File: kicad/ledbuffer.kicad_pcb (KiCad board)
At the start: 2 copper layers, 39.4 x 52.1 mm, 0 parts

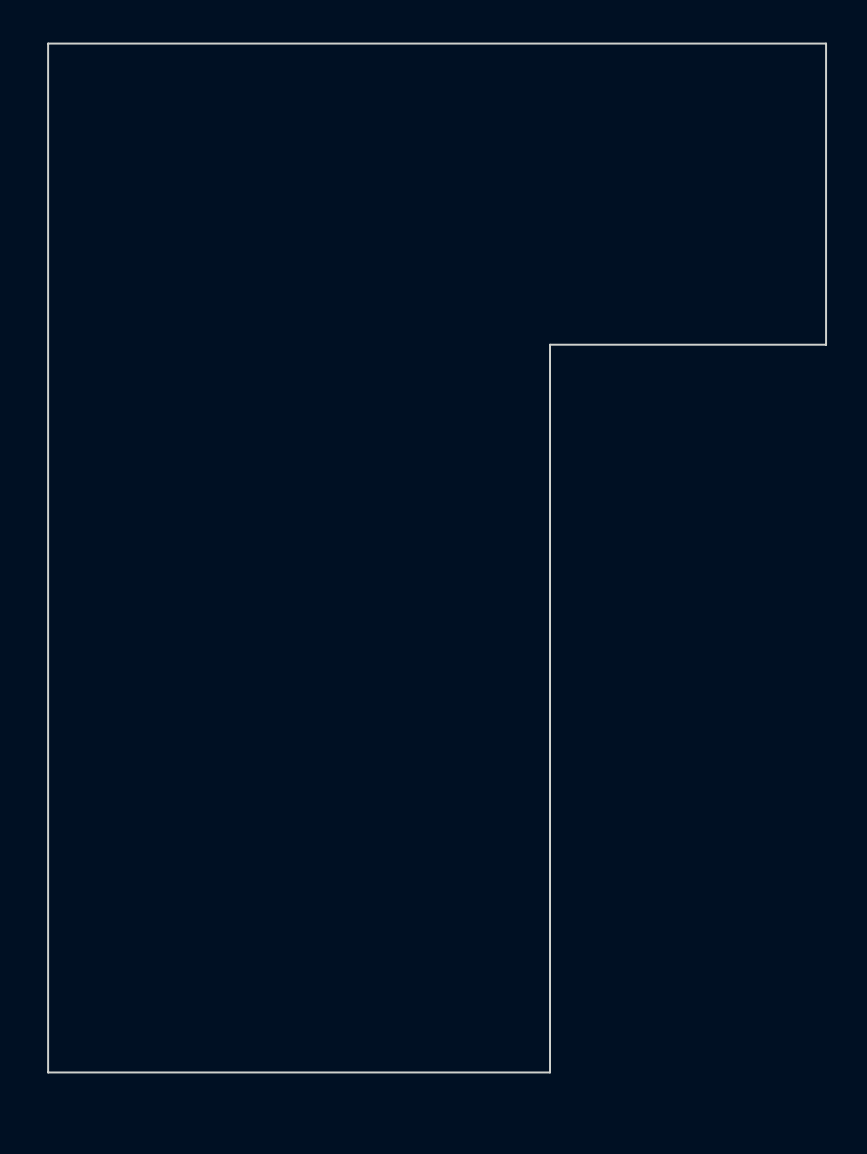
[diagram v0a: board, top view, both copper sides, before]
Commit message: started layout placement by Dharma
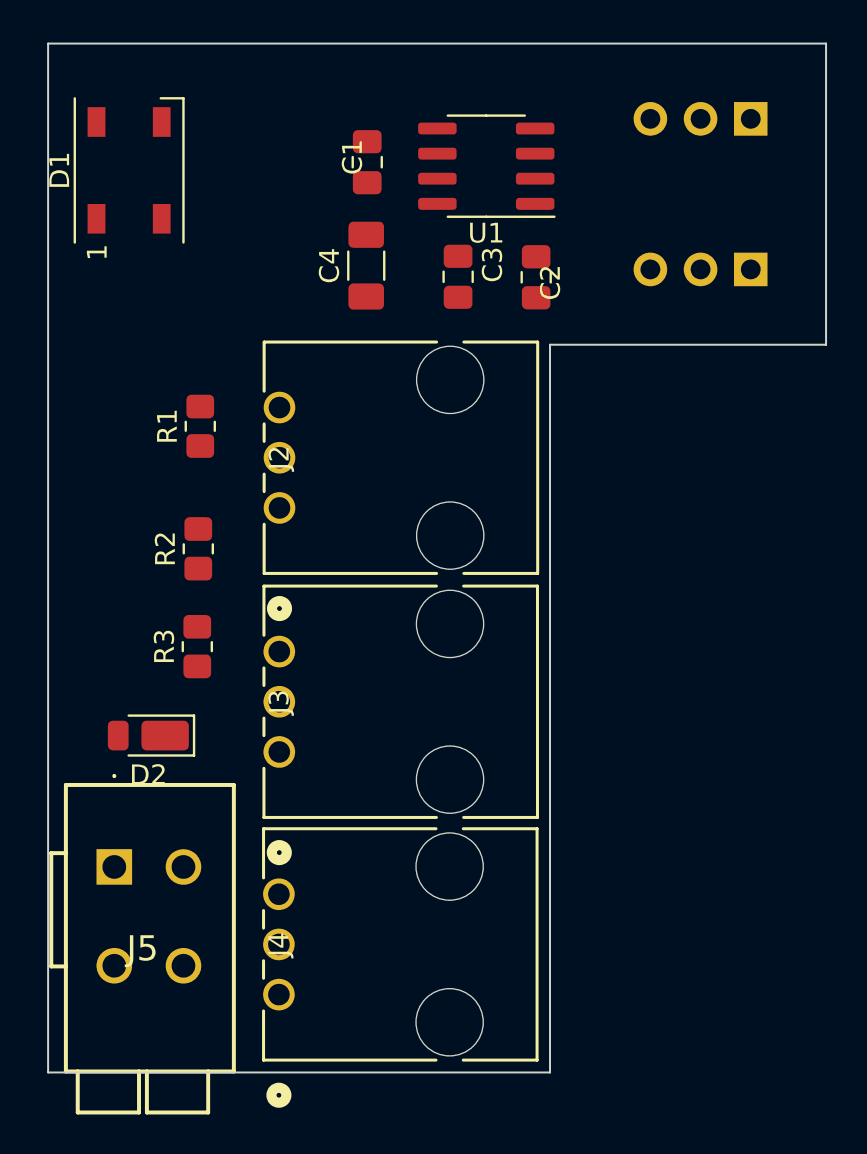
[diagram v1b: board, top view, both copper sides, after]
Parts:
- added C1: 1uF, Capacitor_SMD:C_0805_2012Metric_Pad1.18x1.45mm_HandSolder, F.Cu at (130.4, 55.5)
- added C2: 1uF, Capacitor_SMD:C_0805_2012Metric_Pad1.18x1.45mm_HandSolder, F.Cu at (139.0, 61.4)
- added C3: 1uF, Capacitor_SMD:C_0805_2012Metric_Pad1.18x1.45mm_HandSolder, F.Cu at (135.1, 61.3)
- added C4: 100uF, Capacitor_SMD:C_1206_3216Metric_Pad1.33x1.80mm_HandSolder, F.Cu at (130.4, 60.8)
- added D1: WS2812B, LED_SMD:LED_WS2812B_PLCC4_5.0x5.0mm_P3.2mm, F.Cu at (118.4, 56.0)
- added D2: SBR3U60P1, Diode_SMD:D_PowerDI-123, F.Cu at (119.4, 84.5)
- added J1: Conn_01x03, Connector_PinSocket_2.54mm:PinSocket_1x03_P2.54mm_Vertical, B.Cu at (149.9, 53.3)
- added J2: Conn_01x03, Library:CONN_70555-0002_MOL, F.Cu at (126.0, 73.0)
- added J3: Conn_01x03, Library:CONN_70555-0002_MOL, F.Cu at (126.0, 85.4)
- added J4: Conn_01x03, Library:CONN_70555-0002_MOL, F.Cu at (126.0, 97.7)
- added J5: Conn_01x02, Library:26011102, F.Cu at (117.7, 91.2)
- added J6: Conn_01x03, Connector_PinSocket_2.54mm:PinSocket_1x03_P2.54mm_Vertical, B.Cu at (149.9, 61.0)
- added R1: 100, Resistor_SMD:R_0805_2012Metric_Pad1.20x1.40mm_HandSolder, F.Cu at (122.0, 68.9)
- added R2: 100, Resistor_SMD:R_0805_2012Metric_Pad1.20x1.40mm_HandSolder, F.Cu at (121.9, 75.1)
- added R3: 100, Resistor_SMD:R_0805_2012Metric_Pad1.20x1.40mm_HandSolder, F.Cu at (121.8, 80.0)
- added U1: LM2931-5.0_SO8, Package_SO:SOIC-8_3.9x4.9mm_P1.27mm, F.Cu at (136.5, 55.7)

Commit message: placement tweaks, set up for routing moved a few things a little bit added net+via sizes and net classes a few sample routes
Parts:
- moved C2 22.4 mm to (118.1, 53.3), turned to 0 degrees
- moved C3 10.9 mm to (127.6, 53.3)
- moved C1 9.51 mm to (139.7, 53.3), turned to -90 degrees
- moved C4 9.13 mm to (125.1, 53.3), turned to -90 degrees
- moved D1 3.74 mm to (118.4, 59.7)
- moved U1 3.32 mm to (133.3, 54.6), turned to 0 degrees
- moved D2 0.73 mm to (119.4, 83.8)
- turned R1 to 0 degrees
- turned R2 to 0 degrees
- turned R3 to 0 degrees
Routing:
- net +6V: track 0.00 -> 13.3 mm
- net GND: track 0.00 -> 7.99 mm
- net Net-(D1-DIN): track 0.00 -> 7.18 mm
- net /Vled: track 0.00 -> 4.97 mm

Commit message: added a wire.
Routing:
- net GND: track 7.99 -> 30.5 mm
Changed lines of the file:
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@@
     (stroke (width 0.15) (type default)) (fill none) (layer "User.2"))
   (segment (start 140.97 50.8) (end 144.78 50.8) (width 0.635) (layer "F.Cu") (net 1))
+  (segment (start 139.065 52.705) (end 140.97 50.8) (width 0.635) (layer "F.Cu") (net 1))
   (segment (start 135.825 52.705) (end 139.065 52.705) (width 0.635) (layer "F.Cu") (net 1))
-  (segment (start 139.065 52.705) (end 140.97 50.8) (width 0.635) (layer "F.Cu") (net 1))
   (segment (start 144.78 50.8) (end 147.32 53.34) (width 0.635) (layer "F.Cu") (net 1))
+  (segment (start 149.86 53.34) (end 149.86 60.96) (width 0.635) (layer "F.Cu") (net 2))
   (segment (start 120.51 99.06) (end 124.46 99.06) (width 0.635) (layer "F.Cu") (net 2))
+  (segment (start 140.0332 54.7107) (end 139.7 54.3775) (width 0.635) (layer "F.Cu") (net 2))
+  (segment (start 148.4893 54.7107) (end 140.0332 54.7107) (width 0.635) (layer "F.Cu") (net 2))
+  (segment (start 149.86 53.34) (end 148.4893 54.7107) (width 0.635) (layer "F.Cu") (net 2))
+  (segment (start 139.7 54.3775) (end 136.2275 54.3775) (width 0.635) (layer "F.Cu") (net 2))
+  (segment (start 136.2275 54.3775) (end 135.825 53.975) (width 0.635) (layer "F.Cu") (net 2))
   (segment (start 117.65 96.2) (end 120.51 99.06) (width 0.635) (layer "F.Cu") (net 2))
   (segment (start 144.78 53.34) (end 139.7 58.42) (width 0.254) (layer "B.Cu") (net 5))

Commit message: wires and text
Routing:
- net Net-(D1-DIN): track 7.18 -> 40.0 mm
- net /Vled: track 4.97 -> 37.6 mm
- net GND: track 30.5 -> 0.00 mm
- net +5V: track 0.00 -> 24.3 mm
- net Net-(D1-DOUT): track 0.00 -> 18.4 mm
- net Net-(J4-Pin_3): track 0.00 -> 13.8 mm, vias 0 -> 1
- net Net-(J3-Pin_3): track 0.00 -> 6.48 mm
- net Net-(J2-Pin_3): track 0.00 -> 3.55 mm
- net +6V: track 13.3 -> 12.4 mm
- added copper zone on B.Cu, net GND
- added copper zone on F.Cu, net GND
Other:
- board text added: "M.I.A. - Jake Donovon /dev/mentor0 - Steve Tell THE G.O.A.T. - Dharma Chari-Letts"

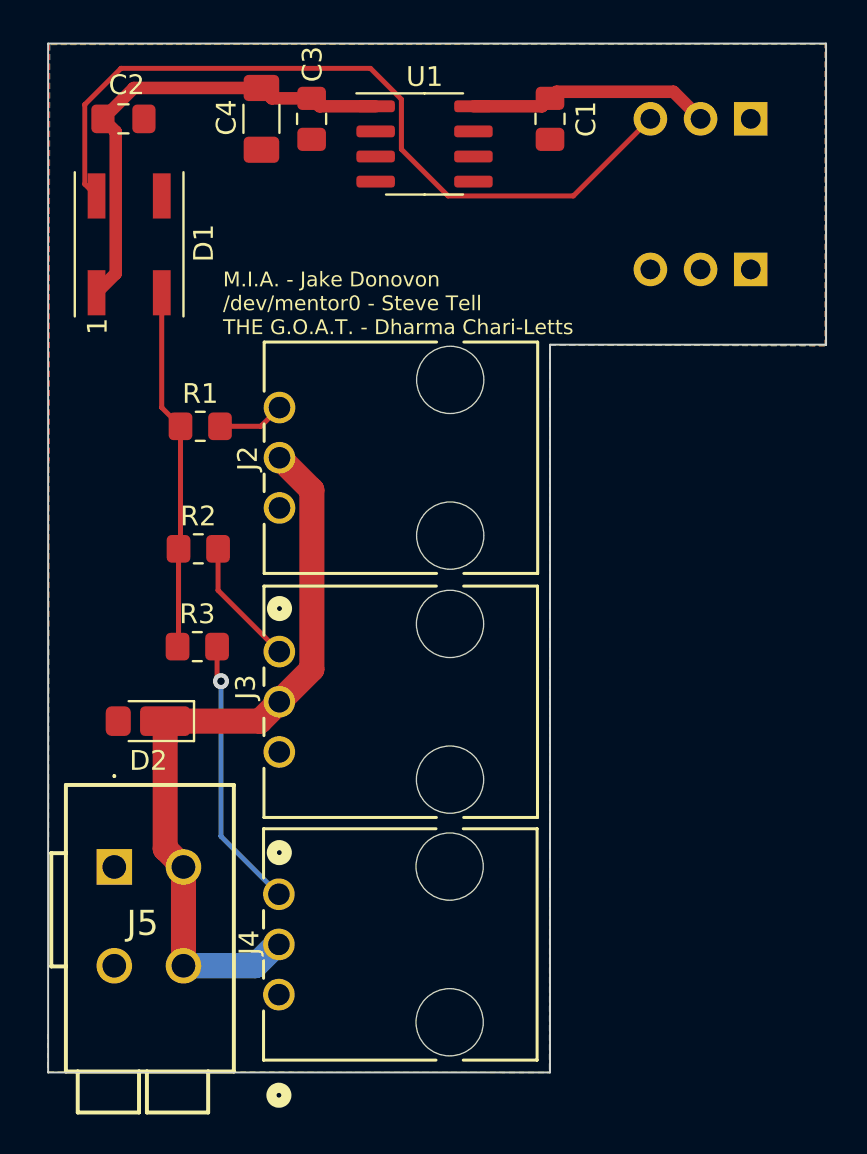
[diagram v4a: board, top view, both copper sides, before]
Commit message: Board Final
Adjusted Placement of R1-3 and Diode
added silkscreen text

Signed-off-by: Jake D <jake@getdonovan.com>
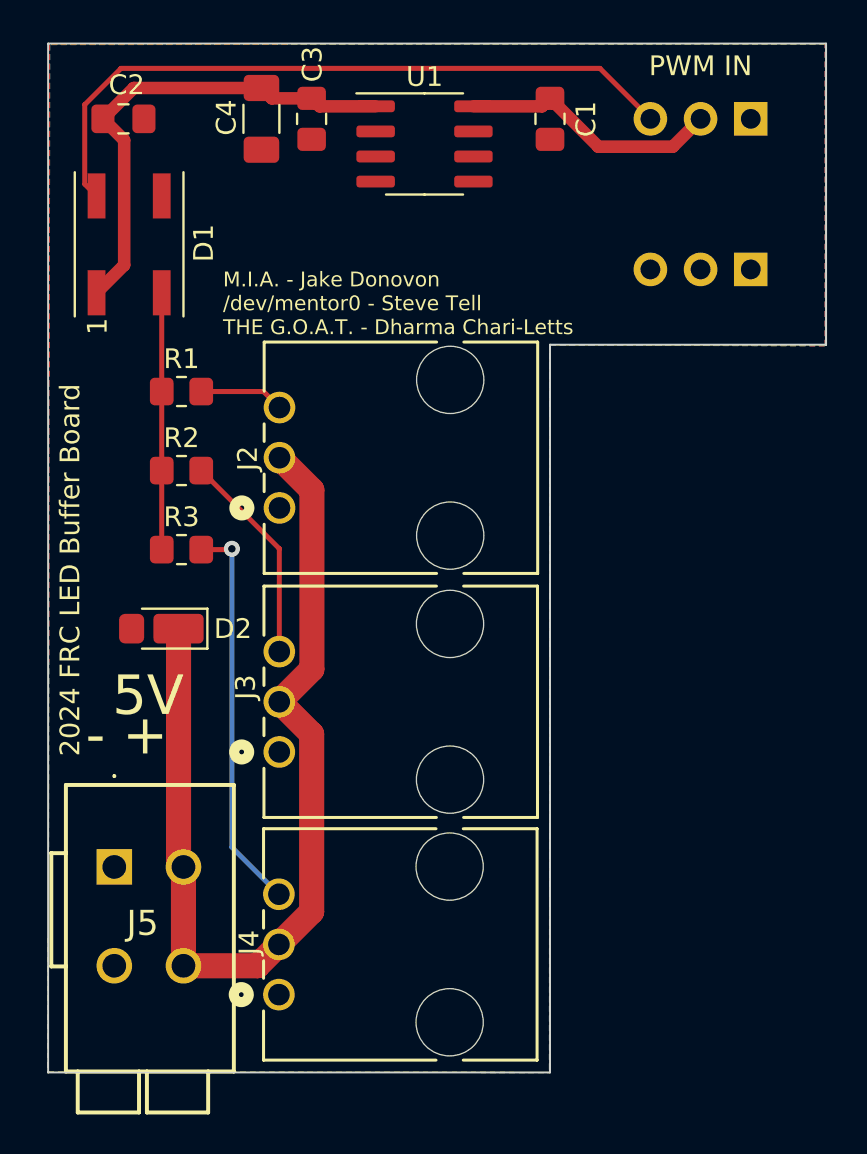
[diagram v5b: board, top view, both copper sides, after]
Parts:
- moved R3 4.97 mm to (121.0, 75.1)
- moved D2 4.73 mm to (120.0, 79.1)
- moved R2 4.05 mm to (121.0, 71.1)
- moved R1 2.00 mm to (121.0, 67.1)
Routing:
- net /Vled: track 37.6 -> 49.8 mm
- net Net-(J4-Pin_3): track 13.8 -> 20.0 mm
- net Net-(D1-DOUT): track 18.4 -> 13.0 mm
- net Net-(D1-DIN): track 40.0 -> 35.3 mm
- net Net-(J3-Pin_3): track 6.48 -> 10.8 mm
- net +6V: track 12.4 -> 13.3 mm
- net Net-(J2-Pin_3): track 3.55 -> 4.30 mm
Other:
- board text added: "- +"
- board text added: "2024 FRC LED Buffer Board"
- board text added: "5V"
- board text added: "PWM IN"

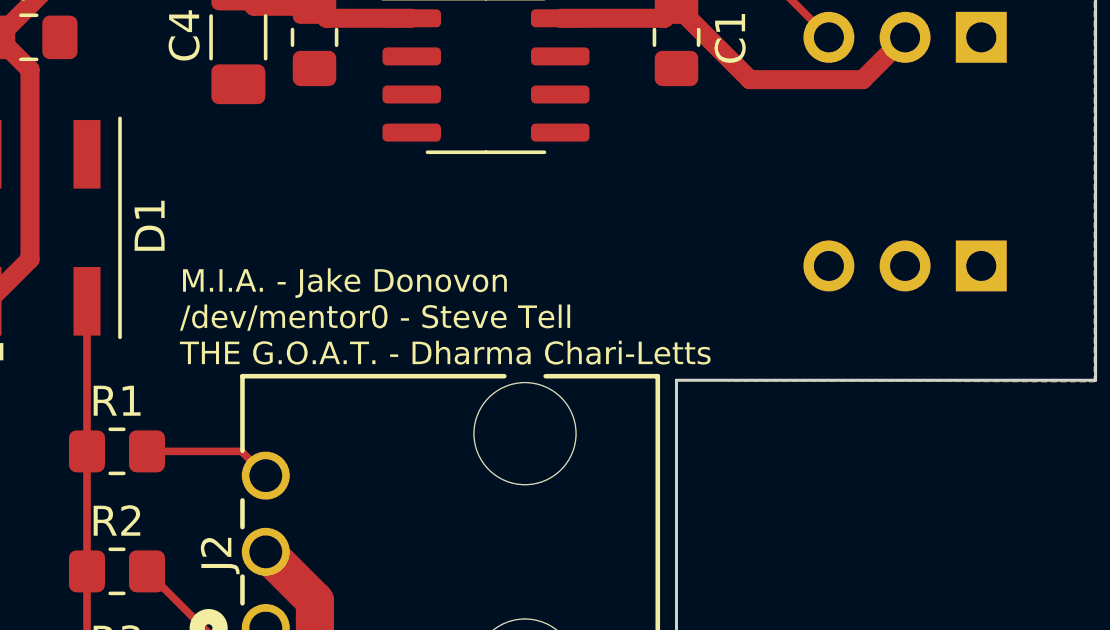
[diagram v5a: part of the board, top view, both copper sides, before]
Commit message: documentation fixes only print out assembly drawing for top layer, add the pdf add pdf of schematic first crack at assembly instructions
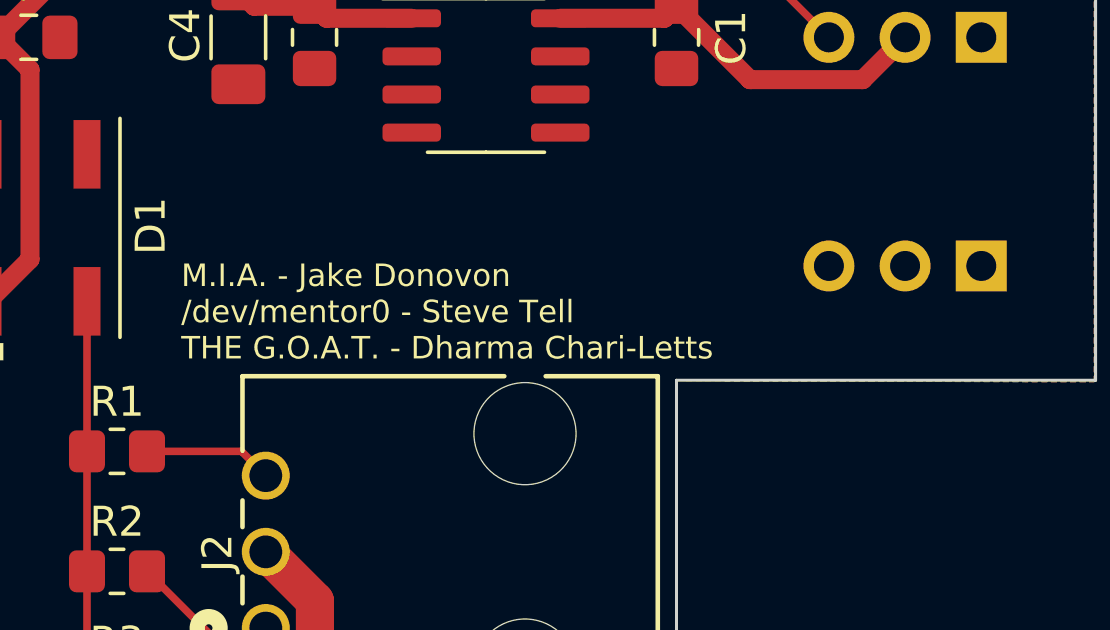
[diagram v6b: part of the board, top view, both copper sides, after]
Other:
- board text added: "2024 LED Buffer Board Team 4795 Eastbots"
- board text added: "5V + -"
- board text added: "<-- LED Power Input <-- 5V Max"
- board text added: "Outputs to WS2812b RGB LED Strips"
- board text added: "PWM in from RoboRIO"
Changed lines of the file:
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@@
         (effects (font (size 1 1) (thickness 0.15)))
     )
-    (fp_text user "${REFERENCE}" (at 0.261252 0.945) (layer "F.Fab")
+    (fp_text user "${REFERENCE}" (at 0 0) (layer "F.Fab")
         (effects (font (size 0.5 0.5) (thickness 0.08)))
     )
@@
         (effects (font (size 1 1) (thickness 0.15)))
     )
-    (fp_text value "100uF" (at 0 0.8 90) (layer "F.Fab")
+    (fp_text value "100uF" (at 4.445 0 90) (layer "F.Fab")
         (effects (font (size 1 1) (thickness 0.15)))
     )
@@
         (effects (font (size 1 1) (thickness 0.15)))
     )
-    (fp_text user "${REFERENCE}" (at 1 0) (layer "F.Fab")
+    (fp_text user "${REFERENCE}" (at 0.108 -0.084) (layer "F.Fab")
         (effects (font (size 0.5 0.5) (thickness 0.08)))
     )
@@
         (effects (font (size 1 1) (thickness 0.15)))
     )
-    (fp_text value "Conn_01x03" (at 2.54 0 90 unlocked) (layer "F.Fab")
-        (effects (font (size 1 1) (thickness 0.15)))
-    )
-    (fp_text user "${REFERENCE}" (at 2.54 0 90 unlocked) (layer "F.Fab")
+    (fp_text value "Conn_01x03" (at 2.418 3.276001 90 unlocked) (layer "F.Fab")
+        (effects (font (size 1 1) (thickness 0.15)))
+    )
+    (fp_text user "${REFERENCE}" (at 2.418 1.752001 90 unlocked) (layer "F.Fab")
         (effects (font (size 1 1) (thickness 0.15)))
     )
@@
         (effects (font (size 1 1) (thickness 0.15)))
     )
-    (fp_text user "${REFERENCE}" (at 1 0) (layer "F.Fab")
+    (fp_text user "${REFERENCE}" (at 0.362 0) (layer "F.Fab")
         (effects (font (size 0.5 0.5) (thickness 0.08)))
     )
@@
         (effects (font (size 1 1) (thickness 0.15)))
     )
-    (fp_text user "${REFERENCE}" (at 2.02 0.64) (layer "F.Fab")
+    (fp_text user "${REFERENCE}" (at 0.108 0.044) (layer "F.Fab")
         (effects (font (size 0.5 0.5) (thickness 0.08)))
     )
@@
         (effects (font (size 1 1) (thickness 0.15)))
     )
-    (fp_text user "${REFERENCE}" (at 2.54 0 90 unlocked) (layer "F.Fab")
+    (fp_text user "${REFERENCE}" (at 2.918 2.798001 90 unlocked) (layer "F.Fab")
         (effects (font (size 1 1) (thickness 0.15)))
     )
@@
         (effects (font (size 1 1) (thickness 0.15)))
     )
-    (fp_text user "${REFERENCE}" (at 0.261252 1.25 90) (layer "F.Fab")
+    (fp_text user "${REFERENCE}" (at 0.261252 0 90) (layer "F.Fab")
         (effects (font (size 0.5 0.5) (thickness 0.08)))
     )
@@
         (effects (font (size 1 1) (thickness 0.15)))
     )
-    (fp_text value "LM2931-5.0_SO8" (at 0 3.4) (layer "F.Fab")
+    (fp_text value "LM2931-5.0_SO8" (at 3.81 3.4) (layer "F.Fab")
         (effects (font (size 1 1) (thickness 0.15)))
     )
@@
         (effects (font (size 1 1) (thickness 0.15)))
     )
-    (fp_text user "${REFERENCE}" (at 2.54 0 90 unlocked) (layer "F.Fab")
+    (fp_text user "${REFERENCE}" (at 2.54 2.524 90 unlocked) (layer "F.Fab")
         (effects (font (size 1 1) (thickness 0.15)))
     )
@@
         (effects (font (size 1 1) (thickness 0.15)))
     )
-    (fp_text value "1uF" (at 0 1.68 90) (layer "F.Fab")
+    (fp_text value "1uF" (at 3.175 0 90) (layer "F.Fab")
         (effects (font (size 1 1) (thickness 0.15)))
     )
@@
   (gr_circle (center 149.86 60.96) (end 150.495 60.96)
     (stroke (width 0.15) (type default)) (fill none) (layer "User.2"))
+  (gr_text "<-- LED Power Input\n<-- 5V Max" (at 118.11 83.82 270) (layer "B.SilkS")
+    (effects (font (size 1.27 1.27) (thickness 0.2032)) (justify left bottom mirror))
+  )
+  (gr_text "2024 LED Buffer Board\nTeam 4795 Eastbots" (at 115.57 59.055) (layer "B.SilkS")
+    (effects (font (size 1.27 1.27) (thickness 0.2032)) (justify right bottom mirror))
+  )
+  (gr_text "PWM in from RoboRIO" (at 142.24 52.705) (layer "B.SilkS")
+    (effects (font (size 1 1) (thickness 0.15)) (justify left bottom mirror))
+  )
+  (gr_text "Outputs to WS2812b RGB LED Strips" (at 137.16 100.33 270) (layer "B.SilkS")
+    (effects (font (size 1.27 1.27) (thickness 0.2032)) (justify left bottom mirror))
+  )
+  (gr_text " 5V\n+ -" (at 122.555 89.535) (layer "B.SilkS")
+    (effects (font (size 1.778 1.778) (thickness 0.2032)) (justify left bottom mirror))
+  )
   (gr_text "- +" (at 116.2 85.7) (layer "F.SilkS")
     (effects (font (size 2 2) (thickness 0.3)) (justify left bottom))
@@
     (effects (font (size 2 2) (thickness 0.3)) (justify left bottom))
   )
-  (gr_text "M.I.A. - Jake Donovon\n/dev/mentor0 - Steve Tell\nTHE G.O.A.T. - Dharma Chari-Letts\n" (at 123.15 64.325) (layer "F.SilkS")
+  (gr_text "M.I.A. - Jake Donovon\n/dev/mentor0 - Steve Tell\nTHE G.O.A.T. - Dharma Chari-Letts\n" (at 123.19 64.135) (layer "F.SilkS")
     (effects (font (size 0.75 0.75) (thickness 0.1125)) (justify left bottom))
   )
